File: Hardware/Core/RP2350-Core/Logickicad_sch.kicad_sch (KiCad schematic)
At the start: 45 parts, among them J7 SWD, J8 USB_C_Receptacle_USB2.0_14P, Q1 BSS123, Q3 BSS123, U1 RP2354B, U19 W25Q16JVSNIQ, U2 AP2112K-3.3, U3 LM66200DRLR, Y1 Crystal

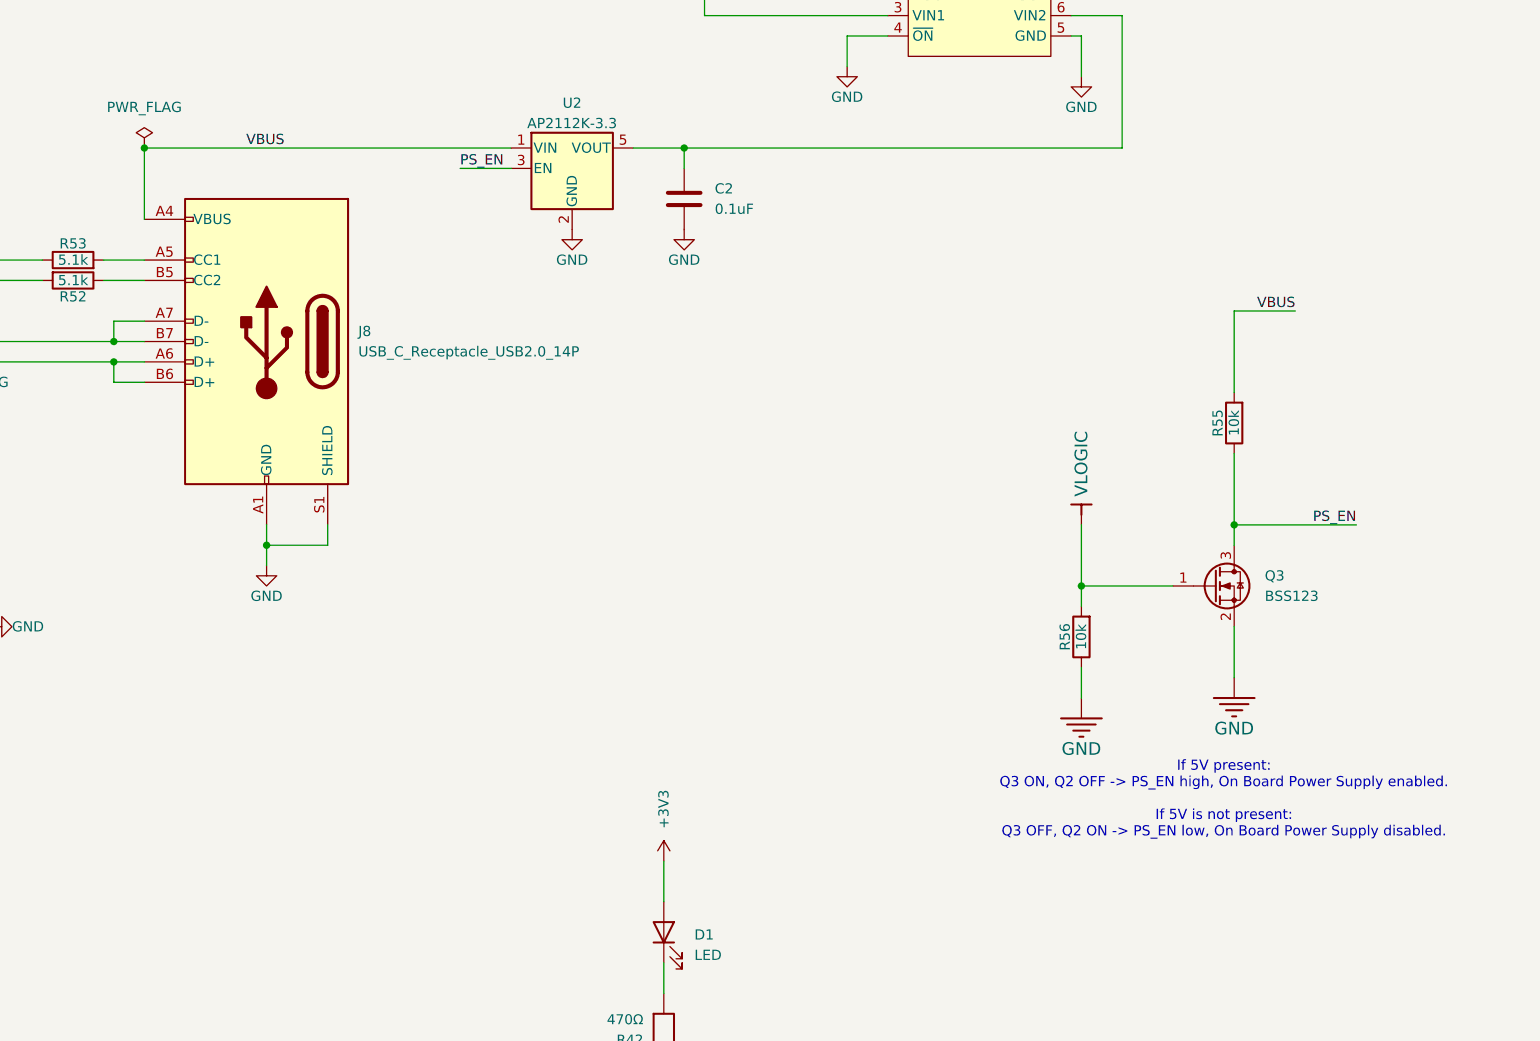
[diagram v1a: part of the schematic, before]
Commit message: Use shared SpaghettiLAB libraries with portable relative paths
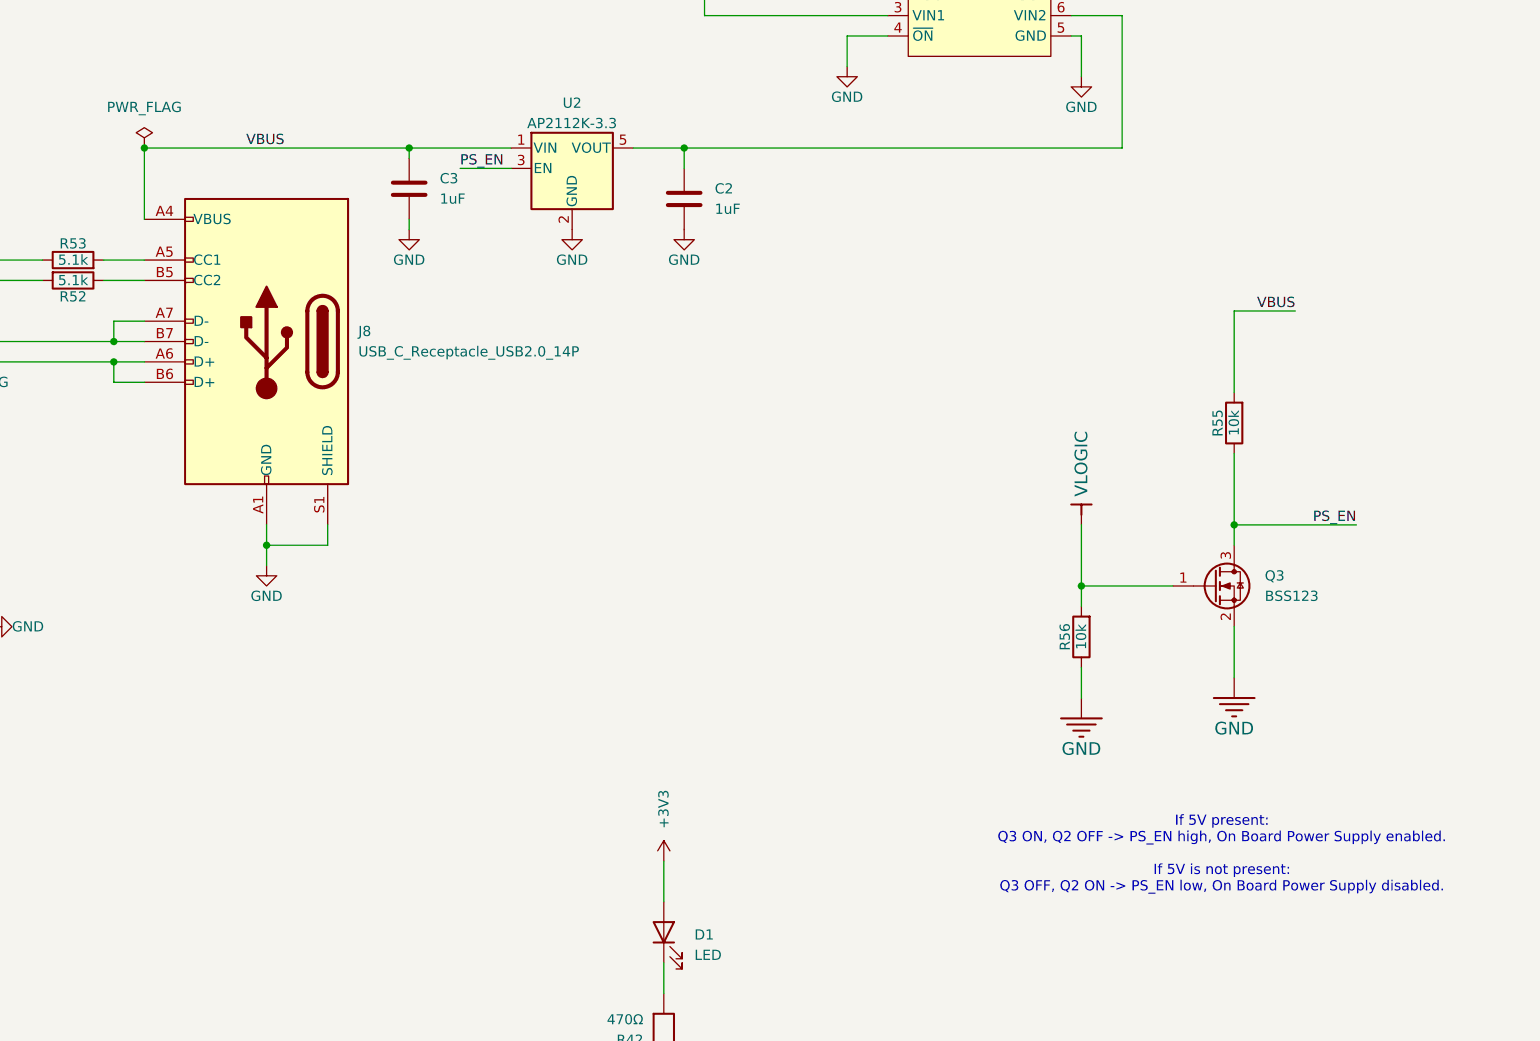
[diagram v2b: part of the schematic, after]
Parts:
- added C3: 1uF, Capacitor_SMD:C_0402_1005Metric, symbol Device:C
- C2: value 0.1uF -> 1uF
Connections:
- net GND: now also C3.1
- net VBUS: now also C3.2
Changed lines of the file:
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@@
 	(text "If 5V present: \nQ3 ON, Q2 OFF -> PS_EN high, On Board Power Supply enabled.\n\nIf 5V is not present:\nQ3 OFF, Q2 ON -> PS_EN low, On Board Power Supply disabled."
 		(exclude_from_sim no)
-		(at 350.52 167.64 0)
+		(at 350.266 174.498 0)
 		(effects
 			(font
@@
 	)
 	(junction
+		(at 248.92 86.36)
+		(diameter 0)
+		(color 0 0 0 0)
+	)
+	(junction
 		(at 72.39 71.12)
 		(diameter 0)
@@
 	(wire
 		(pts
+			(xy 248.92 95.25) (xy 248.92 96.52)
+		)
+		(stroke
+			(width 0)
+			(type default)
+		)
+	)
+	(wire
+		(pts
 			(xy 219.71 27.94) (xy 232.41 27.94)
 		)
@@
 	(wire
 		(pts
-			(xy 215.9 86.36) (xy 261.62 86.36)
+			(xy 215.9 86.36) (xy 248.92 86.36)
 		)
 		(stroke
@@
 	(wire
 		(pts
+			(xy 248.92 86.36) (xy 261.62 86.36)
+		)
+		(stroke
+			(width 0)
+			(type default)
+		)
+	)
+	(wire
+		(pts
 			(xy 85.09 58.42) (xy 124.46 58.42)
 		)
@@
 	(wire
 		(pts
+			(xy 248.92 86.36) (xy 248.92 87.63)
+		)
+		(stroke
+			(width 0)
+			(type default)
+		)
+	)
+	(wire
+		(pts
 			(xy 156.21 39.37) (xy 156.21 38.1)
 		)
@@
 	)
 	(symbol
+		(lib_id "power:GND")
+		(at 248.92 96.52 0)
+		(unit 1)
+		(body_style 1)
+		(exclude_from_sim no)
+		(in_bom yes)
+		(on_board yes)
+		(in_pos_files yes)
+		(dnp no)
+		(property "Reference" "#PWR090"
+			(at 248.92 102.87 0)
+			(hide yes)
+			(show_name no)
+			(do_not_autoplace no)
+			(effects
+				(font
+					(size 1.27 1.27)
+				)
+			)
+		)
+		(property "Value" "GND"
+			(at 248.92 100.33 0)
+			(show_name no)
+			(do_not_autoplace no)
+			(effects
+				(font
+					(size 1.27 1.27)
+				)
+			)
+		)
+		(property "Footprint" ""
+			(at 248.92 96.52 0)
+			(hide yes)
+			(show_name no)
+			(do_not_autoplace no)
+			(effects
+				(font
+					(size 1.27 1.27)
+				)
+			)
+		)
+		(property "Datasheet" ""
+			(at 248.92 96.52 0)
+			(hide yes)
+			(show_name no)
+			(do_not_autoplace no)
+			(effects
+				(font
+					(size 1.27 1.27)
+				)
+			)
+		)
+		(property "Description" ""
+			(at 248.92 96.52 0)
+			(show_name no)
+			(do_not_autoplace no)
+			(effects
+				(font
+					(size 1.27 1.27)
+				)
+			)
+		)
+		(pin "1"
+		)
+		(instances
+			(project "RP2350-Core"
+				(path "/8bfb0932-e2fe-4425-80ff-903dfd664561/72dc90e8-520e-4b34-baab-d68eea14a92b"
+					(reference "#PWR090")
+					(unit 1)
+				)
+			)
+		)
+	)
+	(symbol
 		(lib_id "Connector:USB_C_Receptacle_USB2.0_14P")
 		(at 231.14 110.49 0)
@@
 	)
 	(symbol
+		(lib_id "Device:C")
+		(at 248.92 91.44 180)
+		(unit 1)
+		(body_style 1)
+		(exclude_from_sim no)
+		(in_bom yes)
+		(on_board yes)
+		(in_pos_files yes)
+		(dnp no)
+		(fields_autoplaced yes)
+		(property "Reference" "C3"
+			(at 252.73 90.1699 0)
+			(show_name no)
+			(do_not_autoplace no)
+			(effects
+				(font
+					(size 1.27 1.27)
+				)
+				(justify right)
+			)
+		)
+		(property "Value" "1uF"
+			(at 252.73 92.7099 0)
+			(show_name no)
+			(do_not_autoplace no)
+			(effects
+				(font
+					(size 1.27 1.27)
+				)
+				(justify right)
+			)
+		)
+		(property "Footprint" "Capacitor_SMD:C_0402_1005Metric"
+			(at 247.9548 87.63 0)
+			(hide yes)
+			(show_name no)
+			(do_not_autoplace no)
+			(effects
+				(font
+					(size 1.27 1.27)
+				)
+			)
+		)
+		(property "Datasheet" ""
+			(at 248.92 91.44 0)
+			(hide yes)
+			(show_name no)
+			(do_not_autoplace no)
+			(effects
+				(font
+					(size 1.27 1.27)
+				)
+			)
+		)
+		(property "Description" ""
+			(at 248.92 91.44 0)
+			(show_name no)
+			(do_not_autoplace no)
+			(effects
+				(font
+					(size 1.27 1.27)
+				)
+			)
+		)
+		(property "MFGR" "generic"
+			(at 248.92 91.44 0)
+			(hide yes)
+			(show_name no)
+			(do_not_autoplace no)
+			(effects
+				(font
+					(size 1.27 1.27)
+				)
+			)
+		)
+		(property "MPN" "CL05B104KA5NNNC"
+			(at 248.92 91.44 0)
+			(hide yes)
+			(show_name no)
+			(do_not_autoplace no)
+			(effects
+				(font
+					(size 1.27 1.27)
+				)
+			)
+		)
+		(pin "1"
+		)
+		(pin "2"
+		)
+		(instances
+			(project "RP2350-Core"
+				(path "/8bfb0932-e2fe-4425-80ff-903dfd664561/72dc90e8-520e-4b34-baab-d68eea14a92b"
+					(reference "C3")
+					(unit 1)
+				)
+			)
+		)
+	)
+	(symbol
 		(lib_id "power:GND")
 		(at 156.21 41.91 0)
@@
 			)
 		)
-		(property "Value" "0.1uF"
+		(property "Value" "1uF"
 			(at 287.02 93.9799 0)
 			(show_name no)

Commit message: schematic done, missing pogo expansion pin component selection
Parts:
- removed J8: USB_C_Receptacle_USB2.0_14P, USB-C-Power-tester:TYPE-C-31-M-14, symbol Connector:USB_C_Receptacle_USB2.0_14P
- removed RESET1, USBDEV1: SW_Push, USB-C-Power-tester:SW_Push_1P1T_NO_CK_KMR2, symbol Switch:SW_Push
- added SW1, SW2: TS-1187A-B-A-B, SpaghettiLAB:SW-SMD_4P-L5.1-W5.1-P3.70-LS6.5-TL_H1.5, symbol SpaghettiLab:TS-1187A-B-A-B
- added USBC1: TYPE-C-31-M-14, SpaghettiLAB:USB-C-SMD_12P-P0.50-H-F_TYPE-C-31-M-14, symbol SpaghettiLab:TYPE-C-31-M-14
- C2, C24, C25, C26, C3: footprint Capacitor_SMD:C_0402_1005Metric -> SpaghettiLAB:C0603
- C27, C28, C29, C34, C35, C36, C37, C38, C39, C40, C41: value 0.1uF -> 100nF; footprint Capacitor_SMD:C_0402_1005Metric -> SpaghettiLAB:C0603
- C5, C6: footprint Capacitor_SMD:C_0603_1608Metric -> SpaghettiLAB:C0603
- C58: footprint SpaghettiLAB:C1206 -> SpaghettiLAB:C0603
- D1: footprint (none) -> SpaghettiLAB:LED0603-RD
- Q1, Q3: footprint Package_TO_SOT_SMD:SOT-23 -> SpaghettiLAB:SOT-23-3_L2.9-W1.5-P1.90-LS2.6-BR
- R23, R52, R53, R55, R56, R57: footprint Resistor_SMD:R_0402_1005Metric -> SpaghettiLAB:R0805
- R29, R30, R49, R54: footprint Resistor_SMD:R_0603_1608Metric -> SpaghettiLAB:R0805
- TP4: footprint USBC_PD_mo-easyedapro:Test-Point-0.5mm -> TestPoint:TestPoint_Pad_D2.5mm
- U1: footprint Package_DFN_QFN:QFN-80-1EP_10x10mm_P0.4mm_EP3.4x3.4mm -> SpaghettiLAB:QFN-80_L10.0-W10.0-P0.40-TL-EP3.4
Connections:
- net GND: now also USBC1.A1B12 (GND), USBC1.B1A12 (GND), USBC1.S
- net QSPI_SS: now also SW1.2 (B)
- net USB_DM: now also USBC1.A7 (DN1), USBC1.B7 (DN2)
- net USB_DP: now also USBC1.A6 (DP1), USBC1.B6 (DP2)
- net VBUS: now also USBC1.A4B9 (VBUS), USBC1.B4A9 (VBUS)
- net at R54.1: now also SW1.3 (C)
- net USB_CC1: now reaches R53.2
- net USB_CC1: now also USBC1.A5 (CC1)
- net USB_CC2: now reaches R52.1
- net USB_CC2: now also USBC1.B5 (CC2)
- net at U1.35 (RUN): now also SW2.1 (A)
- net at R29.1: now also SW2.3 (C)
- no-connect marks 5 -> 11
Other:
- moved on the sheet: R54

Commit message: Footprint assigned core rp2350
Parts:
- R23, R29, R30, R42, R46, R47, R49, R52, R53, R54, R55, R56, R57: footprint SpaghettiLAB:R0805 -> SpaghettiLAB:R0603
- U2: footprint Package_TO_SOT_SMD:SOT-23-5 -> SpaghettiLAB:SOT-25-5_L2.9-W1.6-P0.95-LS2.8-BL
- Y1: footprint Crystal:Crystal_SMD_3225-4Pin_3.2x2.5mm -> SpaghettiLAB:CRYSTAL-SMD_4P-L3.2-W2.5-BL
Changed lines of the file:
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@@
 			)
 		)
-		(property "Footprint" "Package_TO_SOT_SMD:SOT-23-5"
+		(property "Footprint" "SpaghettiLAB:SOT-25-5_L2.9-W1.6-P0.95-LS2.8-BL"
 			(at 269.24 80.645 0)
 			(hide yes)
@@
 			)
 		)
-		(property "Footprint" "SpaghettiLAB:R0805"
+		(property "Footprint" "SpaghettiLAB:R0603"
 			(at 353.568 120.65 90)
 			(hide yes)
@@
 			)
 		)
-		(property "Footprint" "SpaghettiLAB:R0805"
+		(property "Footprint" "SpaghettiLAB:R0603"
 			(at 172.72 113.03 0)
 			(hide yes)
@@
 			)
 		)
-		(property "Footprint" "SpaghettiLAB:R0805"
+		(property "Footprint" "SpaghettiLAB:R0603"
 			(at 173.99 67.818 90)
 			(hide yes)
@@
 			)
 		)
-		(property "Footprint" "SpaghettiLAB:R0805"
+		(property "Footprint" "SpaghettiLAB:R0603"
 			(at 251.46 218.44 0)
 			(hide yes)
@@
 			)
 		)
-		(property "Footprint" "SpaghettiLAB:R0805"
+		(property "Footprint" "SpaghettiLAB:R0603"
 			(at 336.042 57.15 90)
 			(hide yes)
@@
 			)
 		)
-		(property "Footprint" "SpaghettiLAB:R0805"
+		(property "Footprint" "SpaghettiLAB:R0603"
 			(at 167.64 151.13 0)
 			(hide yes)
@@
 			)
 		)
-		(property "Footprint" "SpaghettiLAB:R0805"
+		(property "Footprint" "SpaghettiLAB:R0603"
 			(at 215.9 151.13 0)
 			(hide yes)
@@
 			)
 		)
-		(property "Footprint" "Crystal:Crystal_SMD_3225-4Pin_3.2x2.5mm"
+		(property "Footprint" "SpaghettiLAB:CRYSTAL-SMD_4P-L3.2-W2.5-BL"
 			(at 175.895 146.05 0)
 			(hide yes)
@@
 			)
 		)
-		(property "Footprint" "SpaghettiLAB:R0805"
+		(property "Footprint" "SpaghettiLAB:R0603"
 			(at 207.01 101.092 90)
 			(hide yes)
@@
 			)
 		)
-		(property "Footprint" "SpaghettiLAB:R0805"
+		(property "Footprint" "SpaghettiLAB:R0603"
 			(at 172.72 110.49 0)
 			(hide yes)
@@
 			)
 		)
-		(property "Footprint" "SpaghettiLAB:R0805"
+		(property "Footprint" "SpaghettiLAB:R0603"
 			(at 334.518 147.32 90)
 			(hide yes)
@@
 			)
 		)
-		(property "Footprint" "SpaghettiLAB:R0805"
+		(property "Footprint" "SpaghettiLAB:R0603"
 			(at 207.01 102.108 90)
 			(hide yes)
@@
 			)
 		)
-		(property "Footprint" "SpaghettiLAB:R0805"
+		(property "Footprint" "SpaghettiLAB:R0603"
 			(at 280.67 196.85 0)
 			(hide yes)
@@
 			)
 		)
-		(property "Footprint" "SpaghettiLAB:R0805"
+		(property "Footprint" "SpaghettiLAB:R0603"
 			(at 185.42 102.87 0)
 			(hide yes)
